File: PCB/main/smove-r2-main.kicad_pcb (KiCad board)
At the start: 4 copper layers, 25 x 35.5 mm, 49 parts, among them J1 TYPE-C-31-M-12, J2 Battery wire pads 2.54mm, SW2 RESET, SW3 BOOT / USER, U1 ESP32-C3-MINI-1-N4, U2 ICM-20948, U3 PCA9306DCUR, U4 AP2112K-3.3TRG1, U5 AP2112K-1.8TRG1, U6 BQ24074RGTR, U8 USBLC6-2SC6, U9 PESD5V0S2BT,215

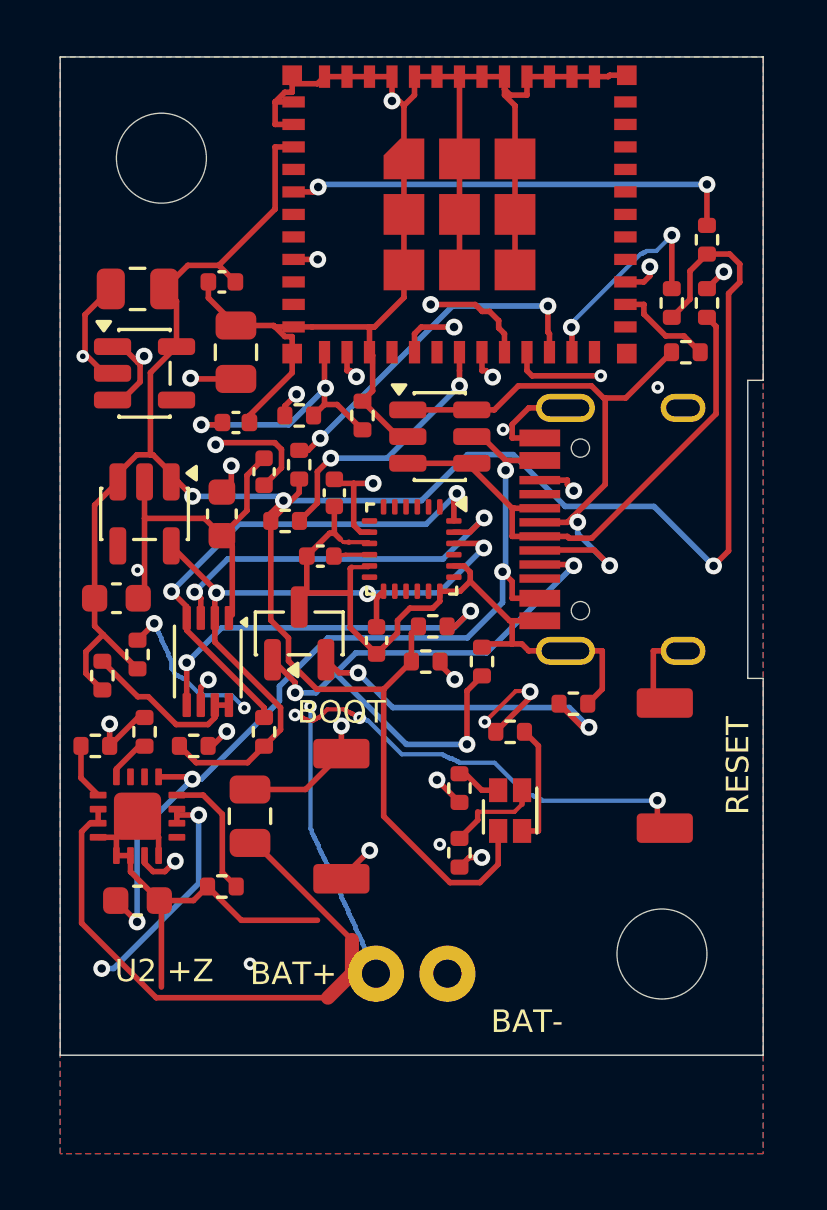
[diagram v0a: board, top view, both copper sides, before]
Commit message: Compact main PCB to 25x30mm with keyed single-M3 housing and validated complete delivery
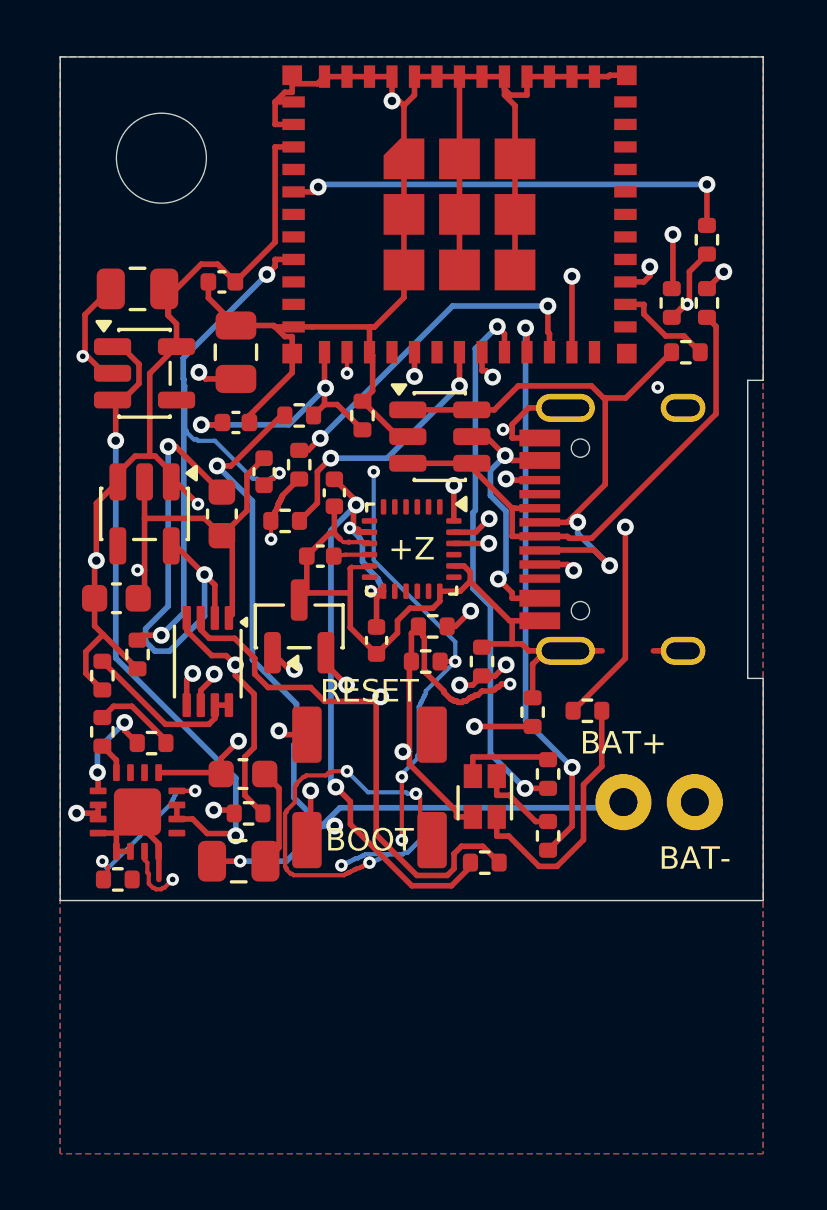
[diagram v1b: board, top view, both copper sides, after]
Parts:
- removed H2: M3 NPTH 3.2mm, MountingHole_3.2mm_M3
- moved R16 11.2 mm to (115.1, 128.7)
- moved J2 10.7 mm to (121.3, 126.5)
- moved SW2 10.6 mm to (111.0, 124.1), turned to 0 degrees
- moved C1 5.86 mm to (106.5, 125.5)
- moved R22 3.71 mm to (102.0, 129.2), turned to 0 degrees
- moved R12 3.21 mm to (117.3, 127.7)
- moved R11 3.19 mm to (117.3, 125.5)
- moved R17 2.95 mm to (106.7, 126.9), turned to 0 degrees
- moved R13 2.85 mm to (118.8, 123.2)
- moved R23 2.00 mm to (103.2, 124.4)
- moved C2 1.65 mm to (106.3, 128.6), turned to 0 degrees
- moved R21 1.50 mm to (101.5, 124.0)
- moved R2 1.48 mm to (116.8, 123.3), turned to 90 degrees
- moved SW3 1.31 mm to (111.0, 127.8), turned to 0 degrees
- moved D1 1.03 mm to (115.1, 126.3)
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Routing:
- net /IMU/1V8_IMU: track 39.0 -> 89.0 mm, vias 5 -> 8
- net Net-(U1-GPIO9_/_BOOT): track 31.2 -> 46.9 mm
- net /Compute/MCU_EN: track 43.8 -> 31.2 mm, vias 7 -> 4
- net /IMU/SCL_1V8: track 20.7 -> 31.1 mm, vias 3 -> 2
- net /Power/SYS: track 38.1 -> 28.6 mm, vias 4 -> 3
- net /Power/PACK_P: track 46.4 -> 55.6 mm, vias 2 -> 4
- net /USB_POWER_N: track 27.6 -> 36.1 mm, vias 3 -> 6
- net /USB/CC1: track 22.9 -> 14.7 mm, vias 3 -> 4
- net GND: track 131.9 -> 137.4 mm
- net /Compute/LED_B_K: track 4.31 -> 9.46 mm
- net /3V3_MAIN: track 91.1 -> 87.3 mm, vias 3 -> 6
- net /VBUS: track 32.1 -> 28.3 mm, vias 4 -> 3
- net /Compute/LED_R: track 23.0 -> 19.4 mm
- net /Compute/LED_G: track 23.7 -> 20.5 mm
- net /USB/CC2: track 22.3 -> 19.7 mm
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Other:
- board size 25 x 35.5 mm -> 25 x 30 mm
- board text added: "+Z"
- board text removed: "BODY"
- board text removed: "U2 +Z"

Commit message: Preserve bounded KiCad routing repair and recover clean PCB-only review with mounting release hold
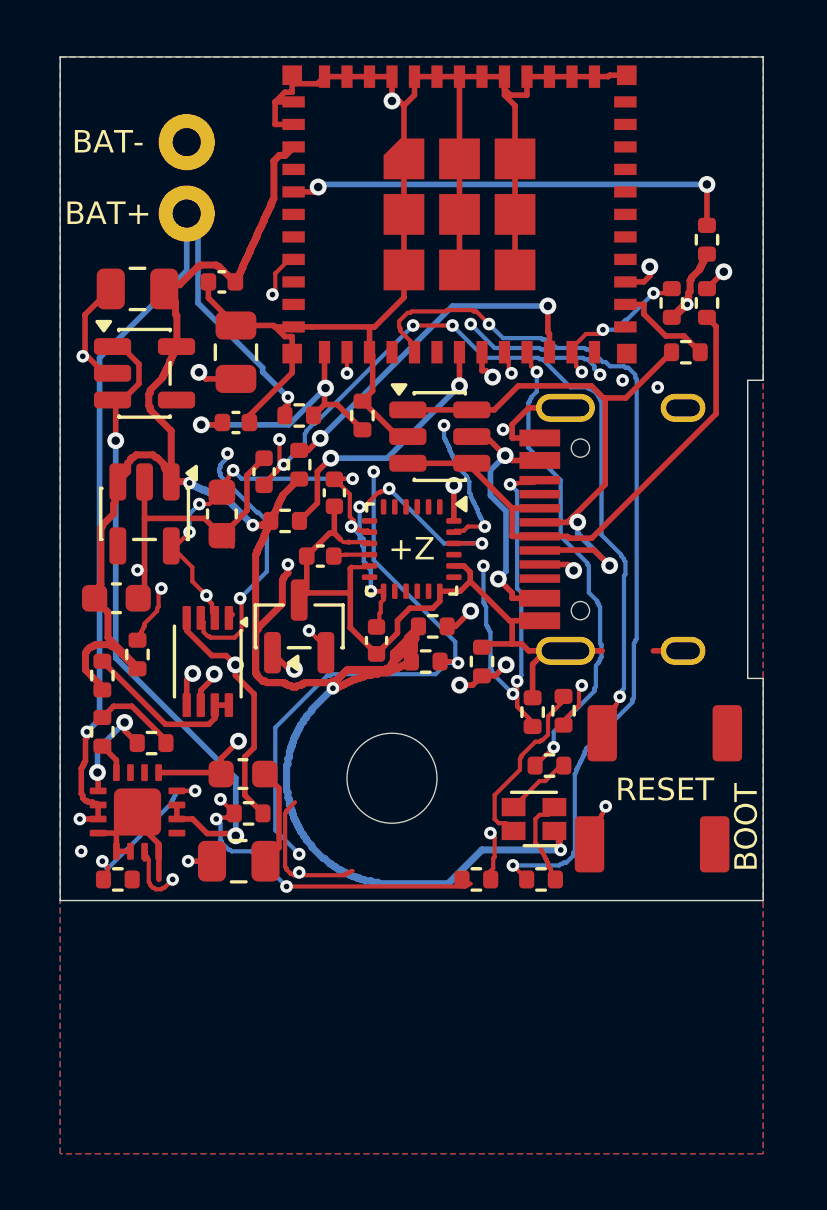
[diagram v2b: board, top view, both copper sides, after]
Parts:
- moved J2 27.8 mm to (104.5, 104.3), turned to 90 degrees
- moved H1 23.5 mm to (111.8, 125.7)
- moved SW2 10.5 mm to (121.5, 124.0)
- moved SW3 10.1 mm to (121.0, 128.0)
- moved R13 6.22 mm to (117.1, 129.2)
- moved R12 2.50 mm to (117.4, 125.2), turned to 0 degrees
- moved R11 2.32 mm to (117.9, 123.2)
- moved D1 1.92 mm to (116.8, 127.1), turned to 90 degrees
- moved R16 0.67 mm to (114.8, 129.2)
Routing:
- net /IMU/1V8_IMU: track 89.0 -> 51.0 mm, vias 8 -> 13
- net /IMU/SCL_1V8: track 31.1 -> 56.5 mm, vias 2 -> 7
- net Net-(U1-GPIO9_/_BOOT): track 46.9 -> 23.3 mm, vias 3 -> 4
- net /3V3_MAIN: track 87.3 -> 108.8 mm
- net /Power/PACK_P: track 55.6 -> 38.2 mm
- net GND: track 137.4 -> 121.4 mm, vias 9 -> 8
- net /Compute/MCU_EN: track 31.2 -> 46.5 mm, vias 4 -> 7
- net /Compute/LED_B: track 19.2 -> 31.9 mm
- net /USB/CC2: track 19.7 -> 26.4 mm, vias 3 -> 5
- net /Compute/LED_B_K: track 9.46 -> 3.66 mm
- net /Compute/LED_R: track 19.4 -> 15.2 mm
- net /Compute/LED_G: track 20.5 -> 17.0 mm
- net /Compute/LED_R_K: track 3.40 -> 6.30 mm
- net /USB_POWER_N: track 36.1 -> 35.1 mm, vias 6 -> 5

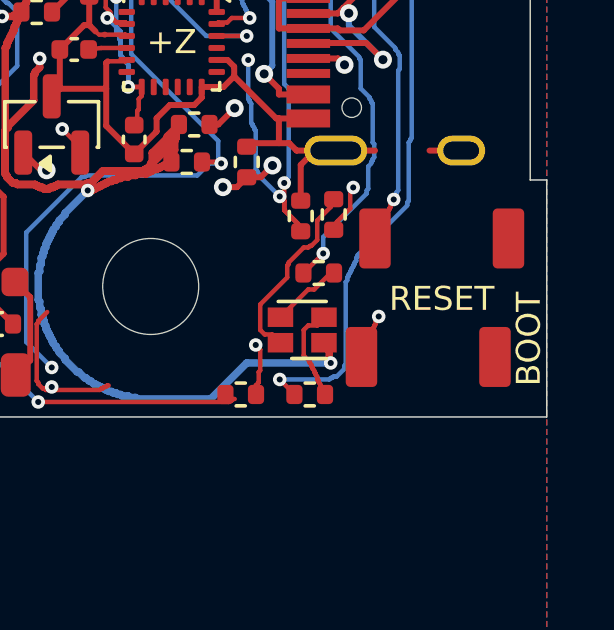
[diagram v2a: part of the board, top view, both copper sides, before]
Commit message: Align buttons.
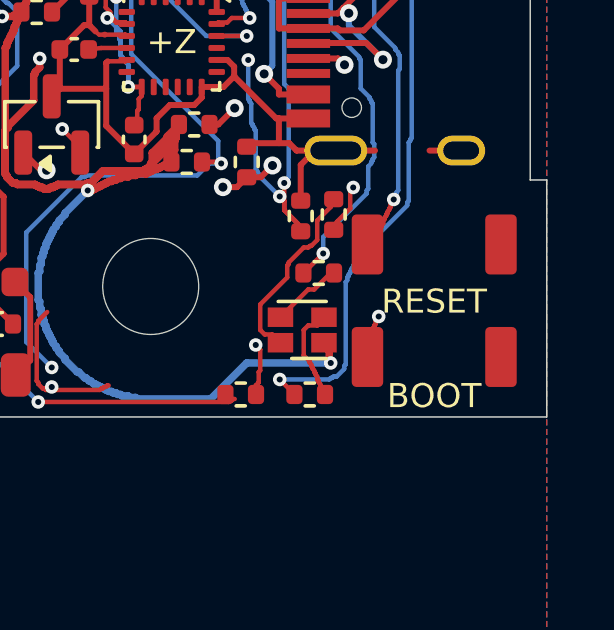
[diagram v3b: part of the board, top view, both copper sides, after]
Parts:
- moved SW2 0.32 mm to (121.2, 124.2)
- moved SW3 0.20 mm to (121.2, 128.0)
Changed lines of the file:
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@@
 	(footprint "smove-r2-main:TS1088"
 		(layer "F.Cu")
-		(at 121.5 124.05)
+		(at 121.25 124.25)
 		(property "Reference" "SW2"
 			(at 0 0 0)
@@
 	(footprint "smove-r2-main:TS1088"
 		(layer "F.Cu")
-		(at 121.05 128)
+		(at 121.25 128)
 		(property "Reference" "SW3"
 			(at 0 0 0)
@@
 	)
 	(gr_text "RESET"
-		(at 121.5 126.06 0)
+		(at 121.25 126.15 0)
 		(layer "F.SilkS")
 		(effects
@@
 	)
 	(gr_text "BOOT"
-		(at 124.4 127.4 90)
+		(at 121.25 129.3 0)
 		(layer "F.SilkS")
 		(effects

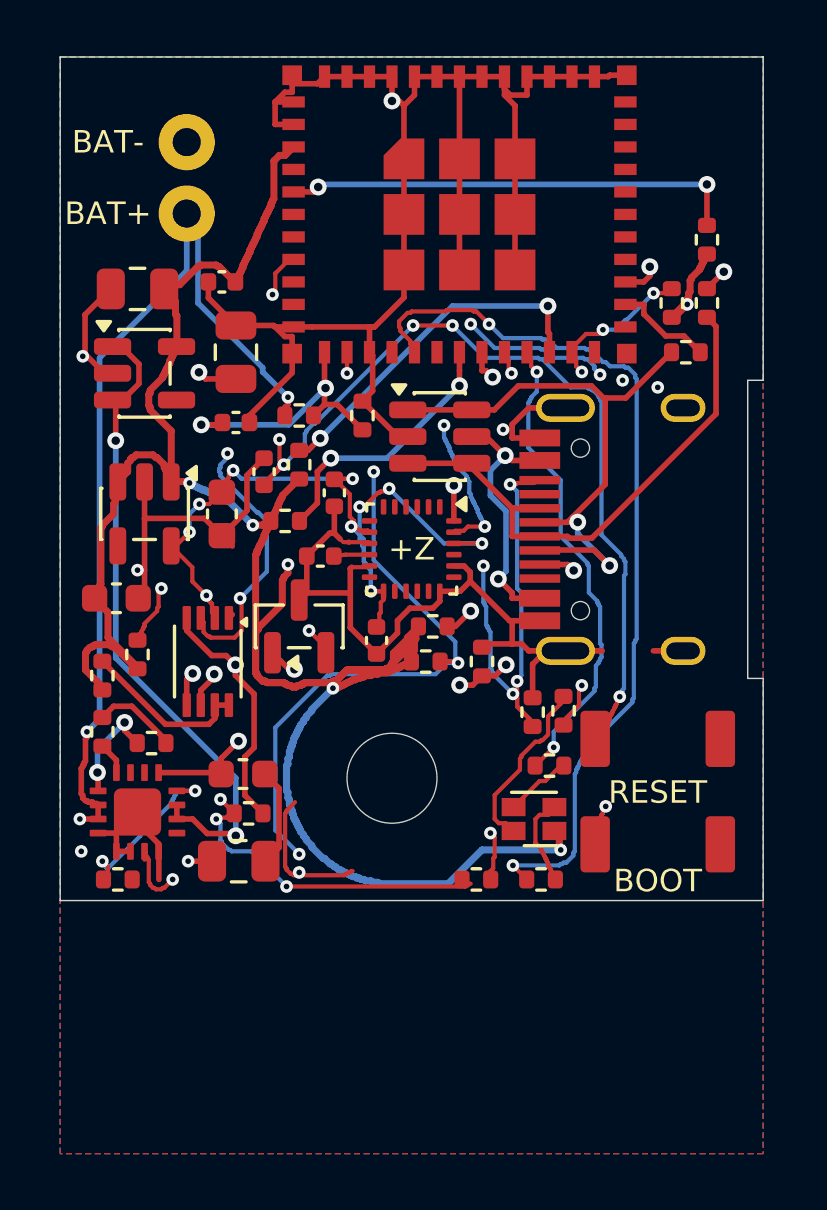
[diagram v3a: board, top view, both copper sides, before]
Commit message: Replace screw mounting with configurable three-piece screwless enclosure and PCB ECO
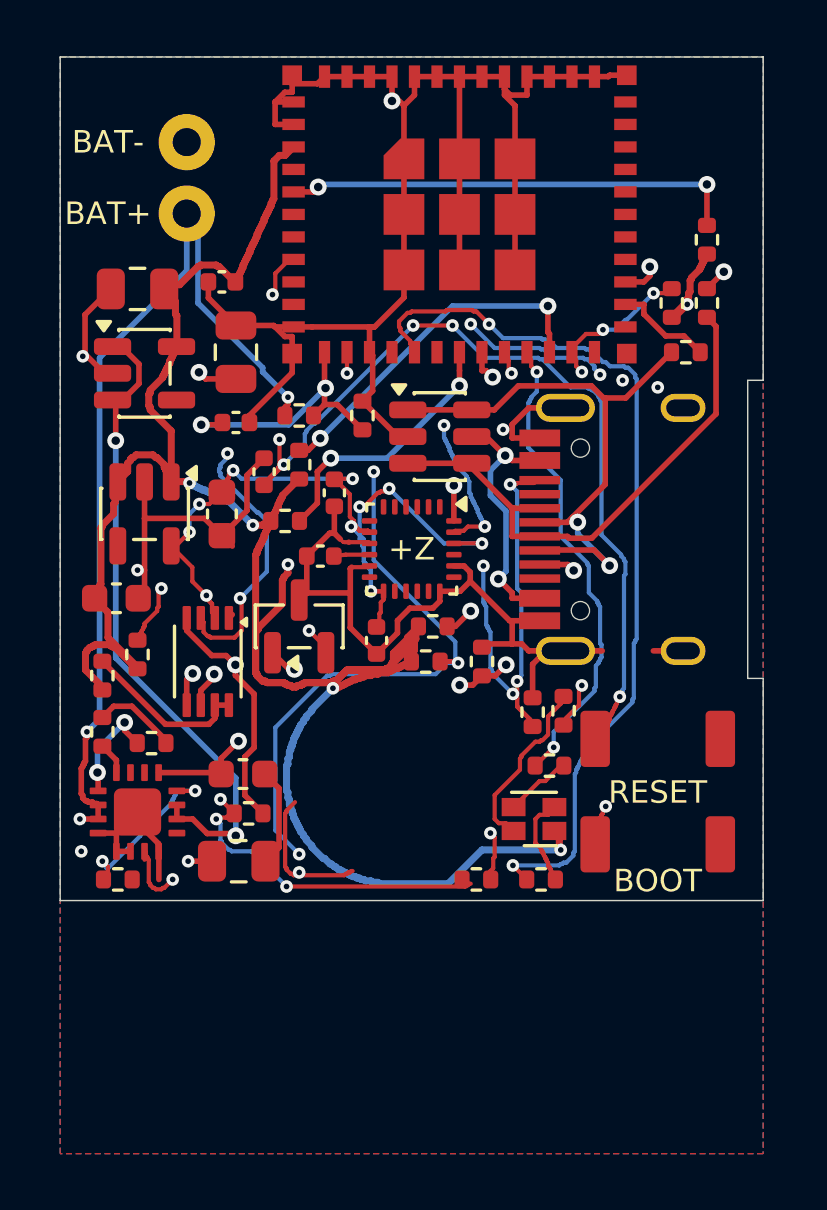
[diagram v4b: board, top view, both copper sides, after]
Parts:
- removed H1: M3 NPTH 3.2mm, MountingHole_3.2mm_M3
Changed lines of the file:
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@@
 		(embedded_fonts no)
 	)
-	(footprint "MountingHole_3.2mm_M3"
-		(layer "F.Cu")
-		(at 111.8 125.65)
-		(property "Reference" "H1"
-			(at 0 0 0)
-			(layer "F.SilkS")
-			(hide yes)
-			(effects
-				(font
-					(size 1.27 1.27)
-					(thickness 0.15)
-				)
-			)
-		)
-		(property "Value" "M3 NPTH 3.2mm"
-			(at 0 0 0)
-			(layer "F.Fab")
-			(hide yes)
-			(effects
-				(font
-					(size 1.27 1.27)
-					(thickness 0.15)
-				)
-			)
-		)
-		(property "Datasheet" ""
-			(at 0 0 0)
-			(layer "F.Fab")
-			(hide yes)
-			(effects
-				(font
-					(size 1.27 1.27)
-					(thickness 0.15)
-				)
-			)
-		)
-		(property "Description" ""
-			(at 0 0 0)
-			(layer "F.Fab")
-			(hide yes)
-			(effects
-				(font
-					(size 1.27 1.27)
-					(thickness 0.15)
-				)
-			)
-		)
-		(attr board_only exclude_from_pos_files exclude_from_bom)
-		(pad "" np_thru_hole circle
-			(at 0 0)
-			(size 3.2 3.2)
-			(drill 3.2)
-			(layers "*.Cu")
-		)
-		(embedded_fonts no)
-	)
 	(footprint "smove-r2-main:SOT-23-5"
 		(layer "F.Cu")
@@
 			)
 		)
-	)
-	(zone
-		(net 0)
-		(net_name "")
-		(layers "F.Cu" "B.Cu" "In1.Cu" "In2.Cu")
-		(name "H1_M3_NO_COPPER")
-		(hatch edge 0.5)
-		(connect_pads
-			(clearance 0)
-		)
-		(min_thickness 0.25)
-		(filled_areas_thickness no)
-		(keepout
-			(tracks not_allowed)
-			(vias not_allowed)
-			(pads allowed)
-			(copperpour not_allowed)
-			(footprints allowed)
-		)
-		(placement
-			(enabled no)
-			(sheetname "")
-		)
-		(fill
-			(thermal_gap 0.5)
-			(thermal_bridge_width 0.5)
-		)
-		(polygon
-			(pts
-				(xy 115.25 125.65) (xy 115.220484 126.100315) (xy 115.132444 126.542925) (xy 114.987384 126.970257)
-				(xy 114.787787 127.374999) (xy 114.537069 127.750226) (xy 114.239518 128.089518) (xy 113.900226 128.387069)
-				(xy 113.524999 128.637787) (xy 113.120257 128.837384) (xy 112.692925 128.982444) (xy 112.250315 129.070484)
-				(xy 111.8 129.1) (xy 111.349684 129.070484) (xy 110.907074 128.982444) (xy 110.479742 128.837384)
-				(xy 110.075 128.637787) (xy 109.699773 128.387069) (xy 109.360481 128.089518) (xy 109.06293 127.750226)
-				(xy 108.812212 127.374999) (xy 108.612615 126.970257) (xy 108.467555 126.542925) (xy 108.379515 126.100315)
-				(xy 108.349999 125.65) (xy 108.379515 125.199684) (xy 108.467555 124.757074) (xy 108.612615 124.329742)
-				(xy 108.812212 123.925) (xy 109.06293 123.549773) (xy 109.360481 123.210481) (xy 109.699773 122.91293)
-				(xy 110.074999 122.662212) (xy 110.479742 122.462615) (xy 110.907074 122.317555) (xy 111.349684 122.229515)
-				(xy 111.8 122.199999) (xy 112.250315 122.229515) (xy 112.692925 122.317555) (xy 113.120257 122.462615)
-				(xy 113.524999 122.662212) (xy 113.900226 122.91293) (xy 114.239518 123.210481) (xy 114.537069 123.549773)
-				(xy 114.787787 123.924999) (xy 114.987384 124.329742) (xy 115.132444 124.757074) (xy 115.220484 125.199684)
-			)
-		)

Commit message: Add a different routing setup
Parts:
- moved J2 18.0 mm to (122.5, 103.2)
- moved R2 8.50 mm to (108.3, 123.4), turned to -90 degrees
- moved R11 8.40 mm to (109.5, 123.4), turned to -90 degrees
- moved D1 7.21 mm to (109.7, 126.0)
- moved R12 6.93 mm to (110.7, 123.4), turned to -90 degrees
- moved R13 6.62 mm to (110.5, 128.7), turned to 90 degrees
- moved SW2 6.53 mm to (114.7, 124.5)
- moved SW3 6.53 mm to (114.7, 128.1)
- moved R16 5.43 mm to (109.4, 128.7), turned to 90 degrees
- moved R9 0.71 mm to (122.5, 107.0), turned to 0 degrees
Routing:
- net /3V3_MAIN: track 108.8 -> 81.1 mm
- net /Compute/LED_B: track 31.9 -> 4.90 mm, vias 2 -> 1
- net Net-(U1-GPIO9_/_BOOT): track 23.3 -> 44.6 mm
- net /Power/PACK_P: track 38.2 -> 55.4 mm, vias 4 -> 3
- net /Compute/LED_G: track 17.0 -> 1.42 mm
- net /Compute/LED_R: track 15.2 -> 0.74 mm, vias 2 -> 1
- net /IMU/SCL_1V8: track 56.5 -> 68.5 mm
- net /Compute/MCU_EN: track 46.5 -> 53.0 mm
- net /IMU/1V8_IMU: track 51.0 -> 45.9 mm
- net /USB/CC2: track 26.4 -> 22.4 mm, vias 5 -> 4
- net /Compute/LED_R_K: track 6.30 -> 3.53 mm
- net /Compute/STRAP2: track 16.3 -> 18.0 mm
- net GND: track 121.4 -> 122.1 mm, vias 8 -> 7
- net /Compute/USB_DP_MCU: track 5.30 -> 5.85 mm
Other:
- board text added: "+"
- board text added: "-"
- board text removed: "BAT+"
- board text removed: "BAT-"

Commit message: Fix routing issues.
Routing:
- net /Compute/LED_B: track 4.90 -> 35.4 mm, vias 1 -> 2
- net /Compute/LED_G: track 1.42 -> 28.7 mm
- net /Compute/LED_R: track 0.74 -> 21.8 mm, vias 1 -> 3
- net Net-(U1-GPIO9_/_BOOT): track 44.6 -> 27.4 mm, vias 4 -> 3
- net GND: vias 7 -> 8

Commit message: Add better component placements for efficient routing.
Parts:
- moved SW2 19.5 mm to (102.4, 109.3), turned to 90 degrees
- moved R8 19.2 mm to (105.2, 118.5), turned to 0 degrees
- moved SW3 17.7 mm to (102.4, 115.5), turned to 90 degrees
- moved R9 15.8 mm to (106.8, 105.4), turned to 90 degrees
- moved D1 13.4 mm to (105.7, 113.2)
- moved R7 12.7 mm to (106.2, 109.0), turned to 0 degrees
- moved R21 12.7 mm to (114.0, 122.4)
- moved R13 12.5 mm to (105.2, 117.4), turned to 0 degrees
- moved C2 12.3 mm to (114.8, 119.6), turned to 90 degrees
- moved C6 11.8 mm to (105.5, 128.0), turned to 0 degrees
- moved U6 11.7 mm to (111.9, 119.5), turned to 180 degrees
- moved R22 11.5 mm to (108.0, 119.5)
- moved C8 11.4 mm to (109.2, 126.9)
- moved C9 10.7 mm to (109.2, 128.4)
- moved C3 10.00 mm to (108.2, 116.6), turned to 0 degrees
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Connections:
- U1 pad 20: /Compute/LED_R -> unconnected-(U1-GPIO6-Pad20)
- U1 pad 6: unconnected-(U1-GPIO3-Pad6) -> /Compute/LED_R
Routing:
- net GND: track 122.1 -> 0.00 mm, vias 8 -> 0
- net /3V3_MAIN: track 81.1 -> 0.00 mm, vias 6 -> 0
- net /IMU/SCL_1V8: track 68.5 -> 0.00 mm, vias 7 -> 0
- net /Power/PACK_P: track 55.4 -> 0.00 mm, vias 3 -> 0
- net /Compute/MCU_EN: track 53.0 -> 0.00 mm, vias 7 -> 0
- net /IMU/1V8_IMU: track 45.9 -> 0.00 mm, vias 13 -> 0
- net /Compute/LED_B: track 35.4 -> 0.00 mm, vias 2 -> 0
- net /USB_POWER_N: track 34.6 -> 0.00 mm, vias 5 -> 0
- net /Compute/LED_G: track 28.7 -> 0.00 mm, vias 2 -> 0
- net /Power/SYS: track 28.6 -> 0.00 mm, vias 3 -> 0
- net /VBUS: track 28.3 -> 0.00 mm, vias 3 -> 0
- net Net-(U1-GPIO9_/_BOOT): track 27.4 -> 0.00 mm, vias 3 -> 0
- net /SDA_HOST: track 23.7 -> 0.00 mm, vias 3 -> 0
- net /USB/CC2: track 22.4 -> 0.00 mm, vias 4 -> 0
- net /Compute/LED_R: track 21.8 -> 0.00 mm, vias 3 -> 0
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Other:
- board text added: "RST"
- board text removed: "RESET"
